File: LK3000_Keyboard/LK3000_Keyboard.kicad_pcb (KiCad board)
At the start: 2 copper layers, 231 x 73 mm, 34 parts, among them J1 Keyboard, SW1 A [MET], SW10 T [+/-], SW11 U [M+], SW12 V [0], SW13 E [7], SW14 F [8], SW15 G [9], SW16 H [÷], SW17 N [4], SW18 O [5], SW19 P [6], SW2 B [US], SW20 Q [+], SW21 W [1], SW22 X [2], SW23 Y [3], SW24 Z [.], SW25 ? [P2}, SW26 bs [P1], SW27 R [-], SW28 I [x], SW29 def [P4], SW3 C [X->M], SW30 stp [P3], SW31 sp [=], SW32 f, SW33 clr, SW4 D [K], SW5 J [C1], SW6 K [C2], SW7 L [RM], SW8 M [%], SW9 S [EXC]

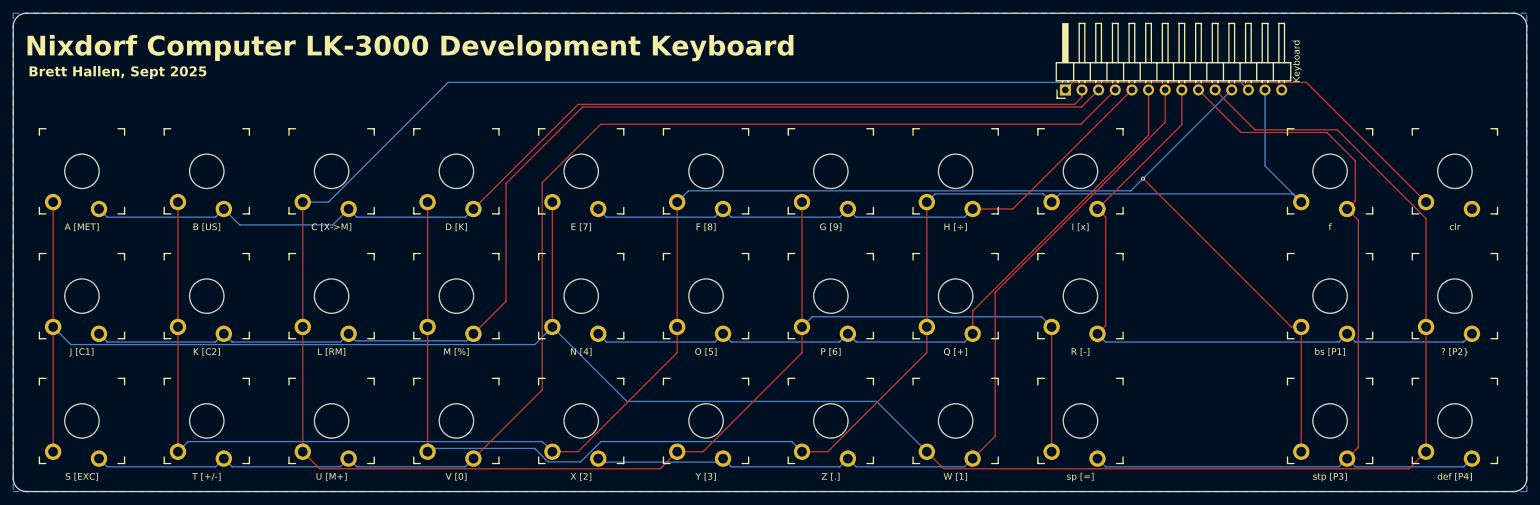
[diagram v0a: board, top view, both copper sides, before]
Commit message: Revised keyboard design to use 12mm tactile
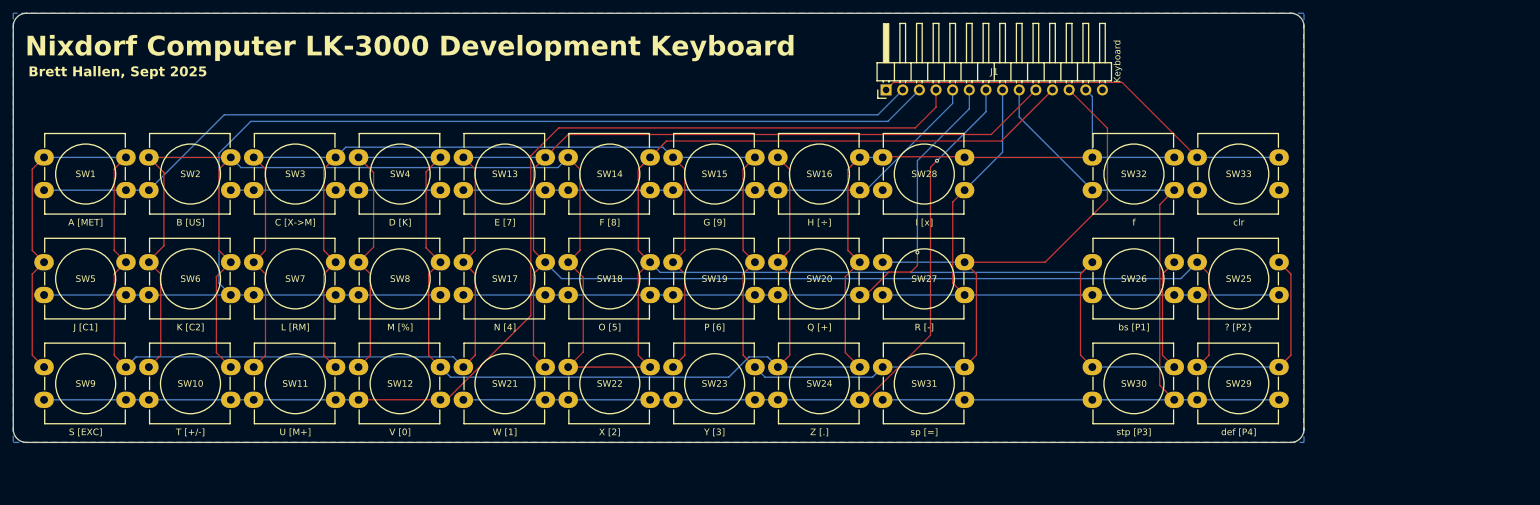
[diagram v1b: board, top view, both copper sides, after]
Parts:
- SW1, SW10, SW11, SW12, SW13, SW14, SW15, SW16, SW17, SW18, SW19, SW2, SW20, SW21, SW22, SW23, SW24, SW25, SW26, SW27, SW28, SW29, SW3, SW30, SW31, SW32, SW33, SW4, SW5, SW6, SW7, SW8, SW9: footprint Clueless_Engineer:SW_Gateron_LowProfile_THT -> Button_Switch_THT:SW_PUSH-12mm_Wuerth-430476085716
- moved SW21 75.6 mm to (93.7, 97.5)
- moved SW29 40.2 mm to (205.7, 97.5)
- moved SW25 39.7 mm to (205.7, 81.5)
- moved SW33 39.4 mm to (205.7, 65.5)
- moved SW30 37.2 mm to (189.7, 97.5)
- moved SW26 36.7 mm to (189.7, 81.5)
- moved SW32 36.3 mm to (189.7, 65.5)
- moved SW31 31.3 mm to (157.7, 97.5)
- moved SW27 30.6 mm to (157.7, 81.5)
- moved SW28 30.3 mm to (157.7, 65.5)
- moved SW20 27.6 mm to (141.7, 81.5)
- moved J1 27.4 mm to (158.2, 55.2)
- moved SW16 27.2 mm to (141.7, 65.5)
- moved SW19 24.6 mm to (125.7, 81.5)
- moved SW15 24.2 mm to (125.7, 65.5)
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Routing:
- net COL2: track 289.1 -> 400.8 mm, vias 1 -> 0
- net COL1: track 354.9 -> 445.9 mm
- net COL4: track 225.1 -> 278.9 mm
- net COL3: track 356.5 -> 326.0 mm
- net ROW3: track 200.0 -> 171.6 mm
- net ROW2: track 181.5 -> 193.8 mm
- net ROW6: track 128.1 -> 116.3 mm, vias 0 -> 1
- net ROW4: track 92.1 -> 82.2 mm
- net ROW8: track 135.0 -> 126.7 mm
- net ROW5: track 108.6 -> 101.2 mm, vias 0 -> 1
- net ROW1: track 162.3 -> 169.4 mm
- net ROW7: track 102.8 -> 95.7 mm
- net ~{CLR}: track 63.1 -> 65.2 mm
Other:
- board size 231 x 73 mm -> 197 x 65.5 mm
